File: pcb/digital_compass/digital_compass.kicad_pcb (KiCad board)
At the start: 2 copper layers, 66 x 66 mm, 10 parts, among them SW1 SW_SPDT, U1 L7805, U2 Seeed Studio XIAO SAMD21, U3 Level_Shifter, U4 QMC5883L, U5 Adafruit_Neopixel_Ring_24

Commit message: Add initial routing for pcb.
This currently passes the existing design rule checks, though I may need
to go back and tweak some placements once I add the JLCPCB-specific
design rules as well.
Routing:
- net GND: track 0.00 -> 141.1 mm, vias 0 -> 1
- net Net-(SW1-A): track 0.00 -> 110.5 mm, vias 0 -> 3
- net Net-(U3-HV2): track 0.00 -> 58.6 mm, vias 0 -> 1
- net Net-(U3-HV1): track 0.00 -> 53.4 mm, vias 0 -> 3
- net Net-(U2-PB08_A6_D6_TX): track 0.00 -> 50.6 mm, vias 0 -> 2
- net Net-(U2-PA9_A5_D5_SCL): track 0.00 -> 46.3 mm, vias 0 -> 2
- net +9V: track 0.00 -> 44.2 mm
- net Net-(U2-PA8_A4_D4_SDA): track 0.00 -> 40.2 mm, vias 0 -> 2
- net Net-(SW1-B): track 0.00 -> 34.7 mm, vias 0 -> 4
- net Net-(U2-3V3): track 0.00 -> 28.3 mm, vias 0 -> 2
- net Net-(U5-Din): track 0.00 -> 17.3 mm
- net Net-(U3-HV3): track 0.00 -> 15.3 mm

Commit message: Update schematic date and add helper silkscreen.
Silkscreen includes ON/OFF for the power switch and project
name/version/author lines.
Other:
- board text added: "Digital Compass v1 Federico Menozzi"
- board text added: "OFF"
- board text added: "ON"
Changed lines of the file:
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@@
     (fp_arc (start -6.9 10.5) (mid -8.301423 9.901423) (end -8.9 8.5)
       (stroke (width 0.12) (type solid)) (layer "F.SilkS"))
-    (fp_arc (start 6.9 -10.5) (mid 8.301492 -9.901492) (end 8.9 -8.5)
+    (fp_arc (start 6.9 -10.5) (mid 8.301494 -9.901494) (end 8.9 -8.5)
       (stroke (width 0.12) (type solid)) (layer "F.SilkS"))
     (fp_arc (start 8.9 8.5) (mid 8.314214 9.914214) (end 6.9 10.5)
@@
   (gr_circle (center 100 100) (end 133 100)
     (stroke (width 0.1) (type default)) (fill none) (layer "Edge.Cuts"))
+  (gr_text "OFF" (at 86.9 121) (layer "F.SilkS")
+    (effects (font (size 1 1) (thickness 0.15)) (justify left bottom))
+  )
+  (gr_text "ON" (at 87.1 110.9) (layer "F.SilkS")
+    (effects (font (size 1 1) (thickness 0.15)) (justify left bottom))
+  )
+  (gr_text "Digital Compass v1\nFederico Menozzi" (at 85.2 107.5) (layer "F.SilkS")
+    (effects (font (size 1 1) (thickness 0.15)) (justify left bottom))
+  )
   (segment (start 75 92.3) (end 79.1 88.2) (width 0.25) (layer "F.Cu") (net 1))
   (segment (start 77.82 104.9825) (end 79.5375 106.7) (width 0.25) (layer "F.Cu") (net 1))

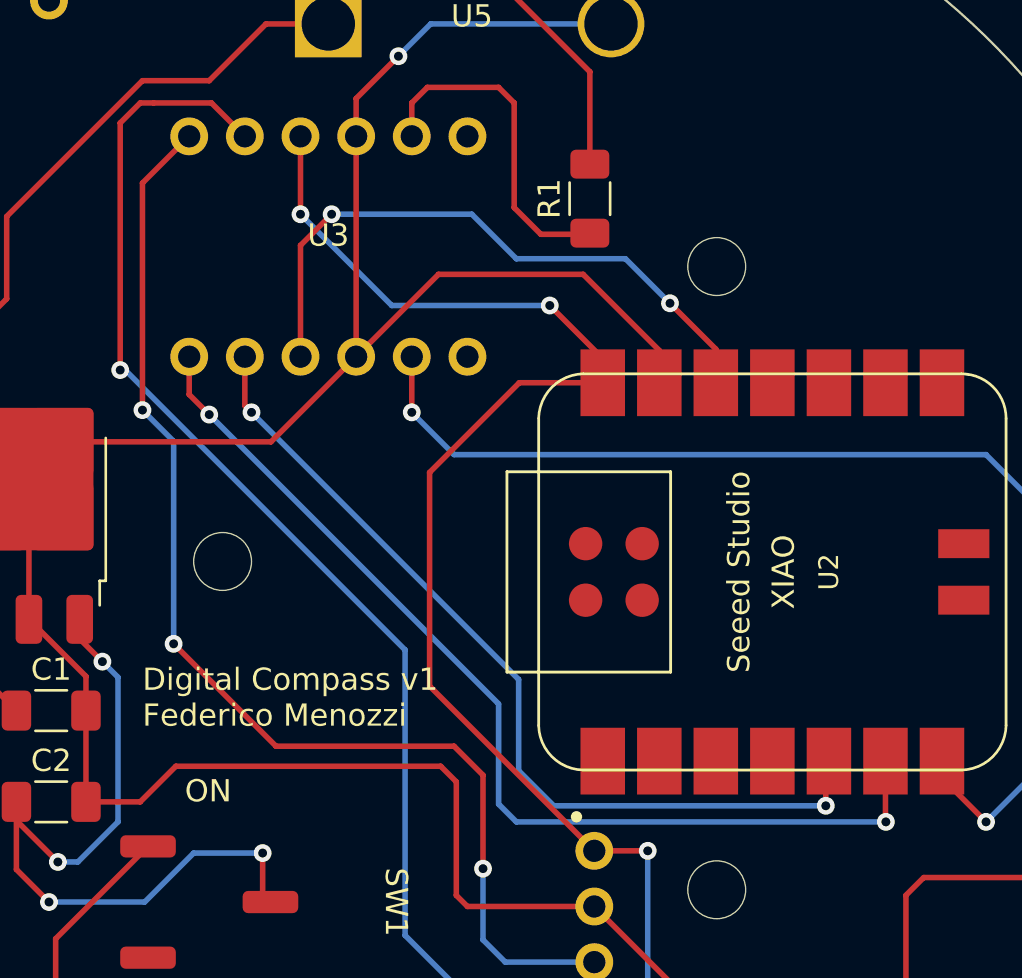
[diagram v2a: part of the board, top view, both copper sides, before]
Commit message: Set up design rules/constraints for jlcpcb.
Taken from https://jlcpcb.com/capabilities/pcb-capabilities.

Also correct two existing DRC violations.
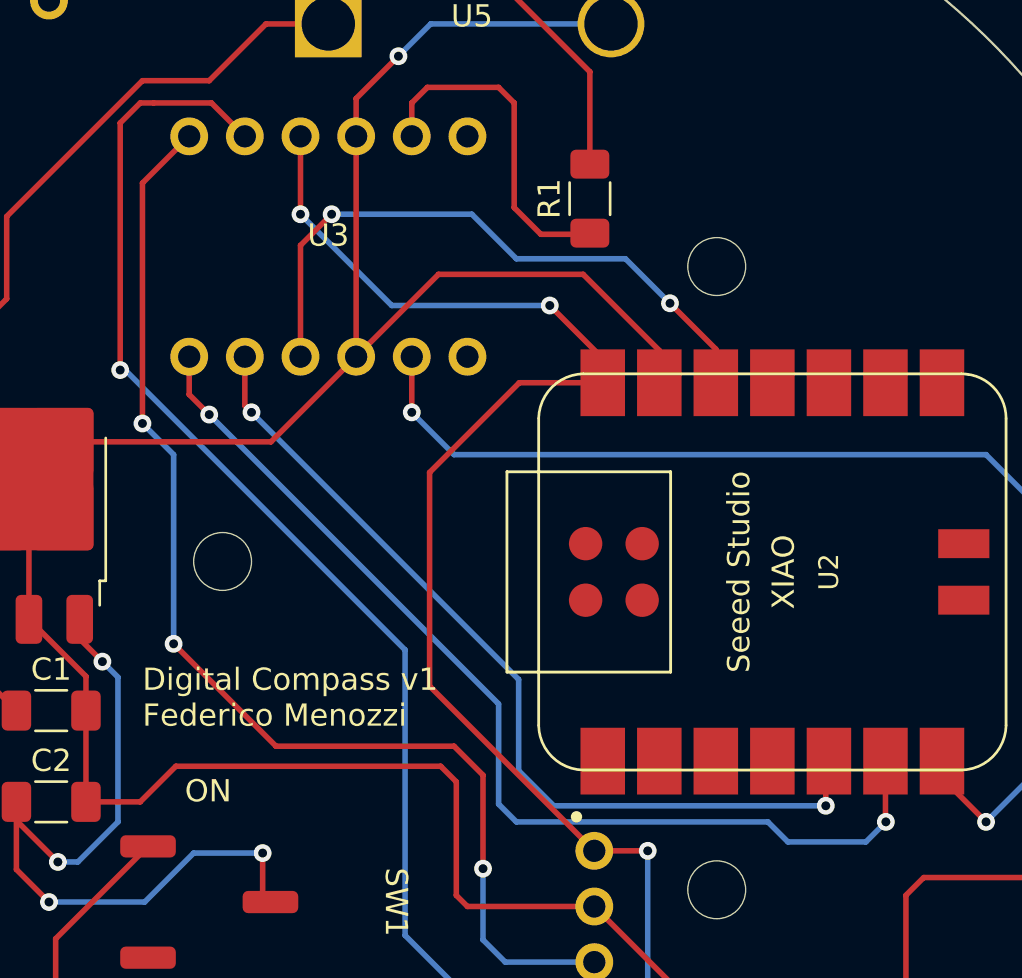
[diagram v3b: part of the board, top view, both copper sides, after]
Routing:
- net Net-(U2-PA9_A5_D5_SCL): track 46.3 -> 47.1 mm
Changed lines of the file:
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@@
   )
   (setup
+    (stackup
+      (layer "F.SilkS" (type "Top Silk Screen"))
+      (layer "F.Paste" (type "Top Solder Paste"))
+      (layer "F.Mask" (type "Top Solder Mask") (thickness 0.01))
+      (layer "F.Cu" (type "copper") (thickness 0.035))
+      (layer "dielectric 1" (type "core") (thickness 1.51) (material "FR4") (epsilon_r 4.5) (loss_tangent 0.02))
+      (layer "B.Cu" (type "copper") (thickness 0.035))
+      (layer "B.Mask" (type "Bottom Solder Mask") (thickness 0.01))
+      (layer "B.Paste" (type "Bottom Solder Paste"))
+      (layer "B.SilkS" (type "Bottom Silk Screen"))
+      (copper_finish "None")
+      (dielectric_constraints no)
+    )
     (pad_to_mask_clearance 0)
     (pcbplotparams
@@
   (via (at 88.2 93.4) (size 0.8) (drill 0.4) (layers "F.Cu" "B.Cu") (net 10))
   (via (at 118.6 111.7) (size 0.8) (drill 0.4) (layers "F.Cu" "B.Cu") (net 10))
+  (segment (start 117.7 112.6) (end 118.6 111.7) (width 0.25) (layer "B.Cu") (net 10))
   (segment (start 101.2 106.4) (end 101.2 110.9) (width 0.25) (layer "B.Cu") (net 10))
-  (segment (start 102 111.7) (end 118.6 111.7) (width 0.25) (layer "B.Cu") (net 10))
+  (segment (start 114.2 112.6) (end 117.7 112.6) (width 0.25) (layer "B.Cu") (net 10))
+  (segment (start 101.2 110.9) (end 102 111.7) (width 0.25) (layer "B.Cu") (net 10))
+  (segment (start 113.3 111.7) (end 114.2 112.6) (width 0.25) (layer "B.Cu") (net 10))
   (segment (start 88.2 93.4) (end 101.2 106.4) (width 0.25) (layer "B.Cu") (net 10))
-  (segment (start 101.2 110.9) (end 102 111.7) (width 0.25) (layer "B.Cu") (net 10))
+  (segment (start 102 111.7) (end 113.3 111.7) (width 0.25) (layer "B.Cu") (net 10))
   (segment (start 121.12 109.72) (end 121.12 108.97) (width 0.25) (layer "F.Cu") (net 11))
   (segment (start 97.3 90.8) (end 97.3 93.3) (width 0.25) (layer "F.Cu") (net 11))
@@
   (segment (start 84.2 91.4) (end 84.425305 91.4) (width 0.25) (layer "B.Cu") (net 25))
   (segment (start 97 103.974695) (end 97 116.8) (width 0.25) (layer "B.Cu") (net 25))
-  (segment (start 87.3 80.9) (end 85.2 83) (width 0.25) (layer "F.Cu") (net 26))
-  (segment (start 85.2 83) (end 85.2 93.2) (width 0.25) (layer "F.Cu") (net 26))
   (segment (start 100.5 109.6) (end 100.5 113.8) (width 0.25) (layer "F.Cu") (net 26))
   (segment (start 86.6 103.7) (end 91.2 108.3) (width 0.25) (layer "F.Cu") (net 26))
   (segment (start 91.2 108.3) (end 99.2 108.3) (width 0.25) (layer "F.Cu") (net 26))
   (segment (start 99.2 108.3) (end 100.5 109.6) (width 0.25) (layer "F.Cu") (net 26))
+  (segment (start 85.2 93.8) (end 85.2 83) (width 0.25) (layer "F.Cu") (net 26))
+  (segment (start 85.2 83) (end 87.3 80.9) (width 0.25) (layer "F.Cu") (net 26))
   (via (at 100.5 113.8) (size 0.8) (drill 0.4) (layers "F.Cu" "B.Cu") (net 26))
-  (via (at 85.2 93.2) (size 0.8) (drill 0.4) (layers "F.Cu" "B.Cu") (net 26))
+  (via (at 85.2 93.8) (size 0.8) (drill 0.4) (layers "F.Cu" "B.Cu") (net 26))
   (via (at 86.6 103.7) (size 0.8) (drill 0.4) (layers "F.Cu" "B.Cu") (net 26))
-  (segment (start 86.6 94.6) (end 86.6 103.7) (width 0.25) (layer "B.Cu") (net 26))
+  (segment (start 85.2 93.8) (end 86.6 95.2) (width 0.25) (layer "B.Cu") (net 26))
   (segment (start 100.5 113.8) (end 100.5 117) (width 0.25) (layer "B.Cu") (net 26))
-  (segment (start 85.2 93.2) (end 86.6 94.6) (width 0.25) (layer "B.Cu") (net 26))
   (segment (start 101.5 118) (end 105.5 118) (width 0.25) (layer "B.Cu") (net 26))
   (segment (start 100.5 117) (end 101.5 118) (width 0.25) (layer "B.Cu") (net 26))
+  (segment (start 86.6 95.2) (end 86.6 103.7) (width 0.25) (layer "B.Cu") (net 26))
   (segment (start 81.3 122.4) (end 88 129.1) (width 0.25) (layer "F.Cu") (net 29))
   (segment (start 85.45 112.8) (end 81.3 116.95) (width 0.25) (layer "F.Cu") (net 29))
